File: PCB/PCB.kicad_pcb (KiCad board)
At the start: 2 copper layers, 76.2 x 55.3 mm, 6 parts, among them U1 Pico

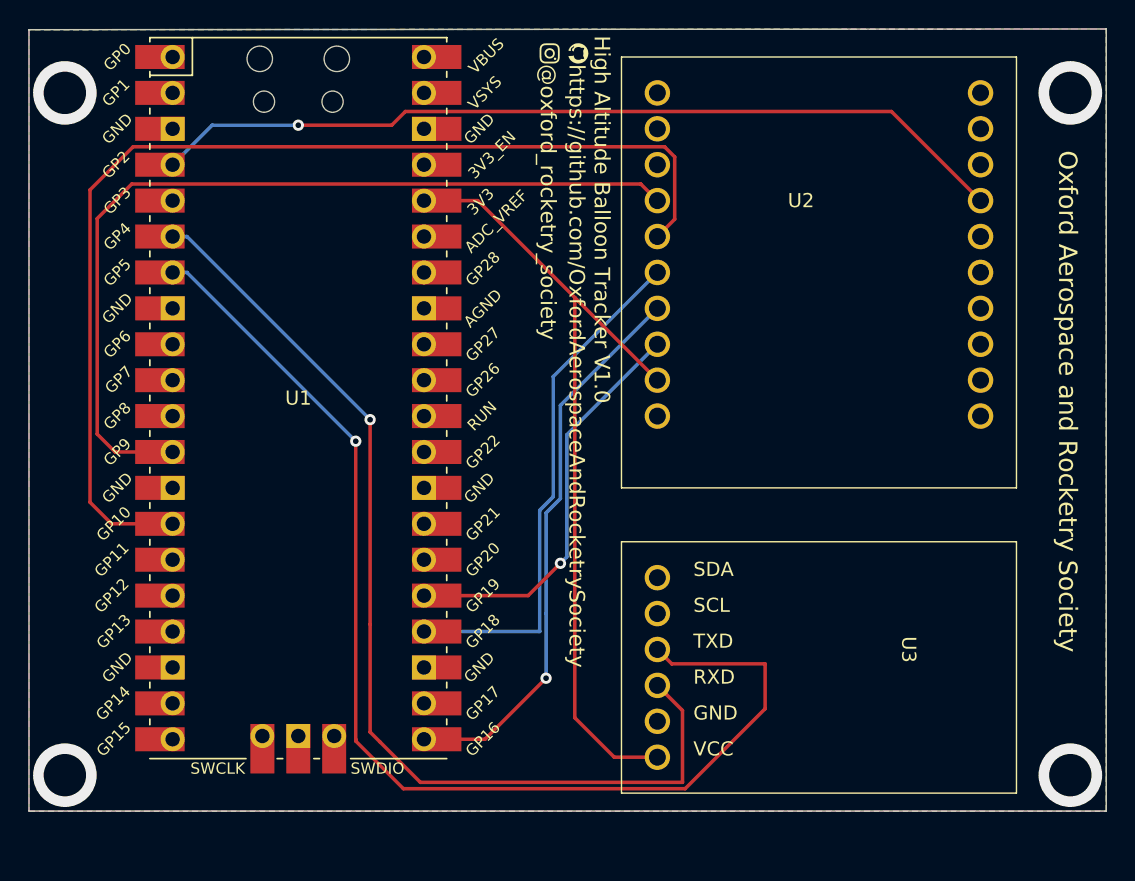
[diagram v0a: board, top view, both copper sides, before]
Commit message: Updated PCB to use SMT RFM9X
PCB now on v1.1, currently untested
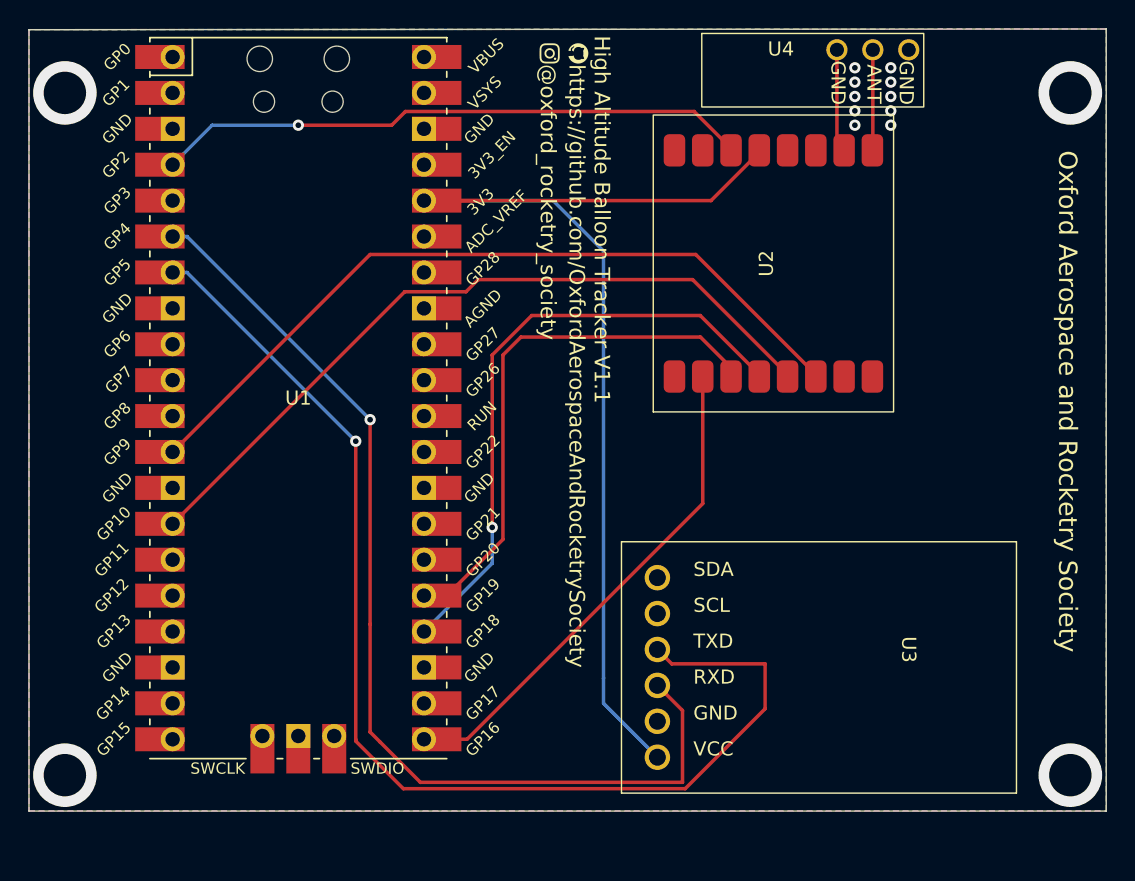
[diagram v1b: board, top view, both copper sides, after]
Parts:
- added U4: ~, RFM9X:Antenna, F.Cu at (156.2, 74.7)
- U2: value ~ -> RFM9X; footprint RFM9X-Breakout:RFM9X -> RFM9X:RFM9X
- moved U2 16.8 mm to (149.2, 93.3), turned to 90 degrees
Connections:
- U2 pad 1: unconnected-(U2-DIO_4-Pad1) -> GND
- U2 pad 11: unconnected-(U2-DIO1-Pad11) -> Net-(U1-GPIO2)
- U2 pad 12: unconnected-(U2-DIO2-Pad12) -> +3V3
- U2 pad 13: Net-(U1-GPIO2) -> unconnected-(U2-DIO4-Pad13)
- U2 pad 15: unconnected-(U2-Pad15) -> GND
- U2 pad 16: unconnected-(U2-Pad16) -> Net-(U2-ANT)
- U2 pad 2: unconnected-(U2-Pad2) -> Net-(U1-GPIO16)
- U2 pad 3: Net-(U1-GPIO9) -> Net-(U1-GPIO19)
- U2 pad 4: Net-(U1-GPIO10) -> Net-(U1-GPIO18)
- U2 pad 5: Net-(U1-GPIO18) -> Net-(U1-GPIO10)
- U2 pad 6: Net-(U1-GPIO16) -> Net-(U1-GPIO9)
- U2 pad 7: Net-(U1-GPIO19) -> unconnected-(U2-DIO5-Pad7)
- U2 pad 8: +3V3 -> GND
- U2 pad 9: GND -> unconnected-(U2-DIO2-Pad9)
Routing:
- net Net-(U1-GPIO10): track 77.6 -> 53.6 mm
- net +3V3: track 58.5 -> 80.6 mm
- net Net-(U1-GPIO2): track 61.3 -> 42.3 mm
- net Net-(U1-GPIO19): track 28.9 -> 38.8 mm, vias 1 -> 0
- net Net-(U1-GPIO18): track 37.0 -> 45.2 mm, vias 0 -> 1
- net GND: track 0.00 -> 7.32 mm
- net Net-(U1-GPIO9): track 62.2 -> 54.9 mm
- net Net-(U2-ANT): track 0.00 -> 7.13 mm
- net Net-(U1-GPIO16): track 39.8 -> 35.6 mm, vias 1 -> 0
- net (no net): vias 4 -> 14
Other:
- board text added: "High Altitude Balloon Tracker V1.1"
- board text removed: "High Altitude Balloon Tracker V1.0"
